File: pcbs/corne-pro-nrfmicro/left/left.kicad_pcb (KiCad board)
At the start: 2 copper layers, 131.6 x 87.7 mm, 53 parts, among them SW1 SW_PUSH-kbd, SW10 SW_PUSH-kbd, SW11 SW_PUSH-kbd, SW12 SW_PUSH-kbd, SW13 SW_PUSH-kbd, SW14 SW_PUSH-kbd, SW15 SW_PUSH-kbd, SW16 SW_PUSH-kbd, SW17 SW_PUSH-kbd, SW18 SW_PUSH-kbd, SW19 SW_PUSH-kbd, SW2 SW_PUSH-kbd, SW20 SW_PUSH-kbd, SW21 SW_PUSH-kbd, SW3 SW_PUSH-kbd, SW4 SW_PUSH-kbd, SW5 SW_PUSH-kbd, SW6 SW_PUSH-kbd, SW7 SW_PUSH-kbd, SW8 SW_PUSH-kbd, SW9 SW_PUSH-kbd, U1 ProMicro-kbd

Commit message: add gerber zip file
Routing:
- net GND: vias 3 -> 5
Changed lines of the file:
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@@
     (pad_to_mask_clearance 0)
     (pcbplotparams
-      (layerselection 0x0001000_7ffffffe)
+      (layerselection 0x00010fc_ffffffff)
       (disableapertmacros false)
-      (usegerberextensions false)
-      (usegerberattributes true)
-      (usegerberadvancedattributes true)
-      (creategerberjobfile true)
+      (usegerberextensions true)
+      (usegerberattributes false)
+      (usegerberadvancedattributes false)
+      (creategerberjobfile false)
       (svguseinch false)
       (svgprecision 6)
@@
       (psnegative false)
       (psa4output false)
-      (plotreference false)
+      (plotreference true)
       (plotvalue false)
       (plotinvisibletext false)
       (sketchpadsonfab false)
-      (subtractmaskfromsilk false)
-      (outputformat 3)
+      (subtractmaskfromsilk true)
+      (outputformat 1)
       (mirror false)
       (drillshape 0)
       (scaleselection 1)
-      (outputdirectory "/home/yong/kbd/split/mykeyboard/corne-pro/case/kicad-primitives/")
+      (outputdirectory "/home/yong/kbd-src/split/mykeyboard/pcbs/corne-pro-nrfmicro/left-gerber/")
     )
   )
@@
   (segment (start 195.208 61.316) (end 195.208 67.892) (width 0.4) (layer "F.Cu") (net 2))
   (segment (start 200.25 72.15) (end 200.25 80.3) (width 0.4) (layer "F.Cu") (net 2))
+  (via (at 200.075 64.275) (size 0.8) (drill 0.4) (layers "F.Cu" "B.Cu") (free) (net 2))
   (via (at 195.2 67.9) (size 0.8) (drill 0.4) (layers "F.Cu" "B.Cu") (net 2))
   (via (at 200.25 72.15) (size 0.8) (drill 0.4) (layers "F.Cu" "B.Cu") (net 2))
+  (via (at 200.075 85.275) (size 0.8) (drill 0.4) (layers "F.Cu" "B.Cu") (free) (net 2))
   (via (at 200.225 105.875) (size 0.8) (drill 0.4) (layers "F.Cu" "B.Cu") (net 2))
   (segment (start 199.75 67.9) (end 200.25 67.4) (width 0.4) (layer "B.Cu") (net 2))

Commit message: backup
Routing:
- net row4: track 81.7 -> 81.1 mm
- net GND: vias 5 -> 6

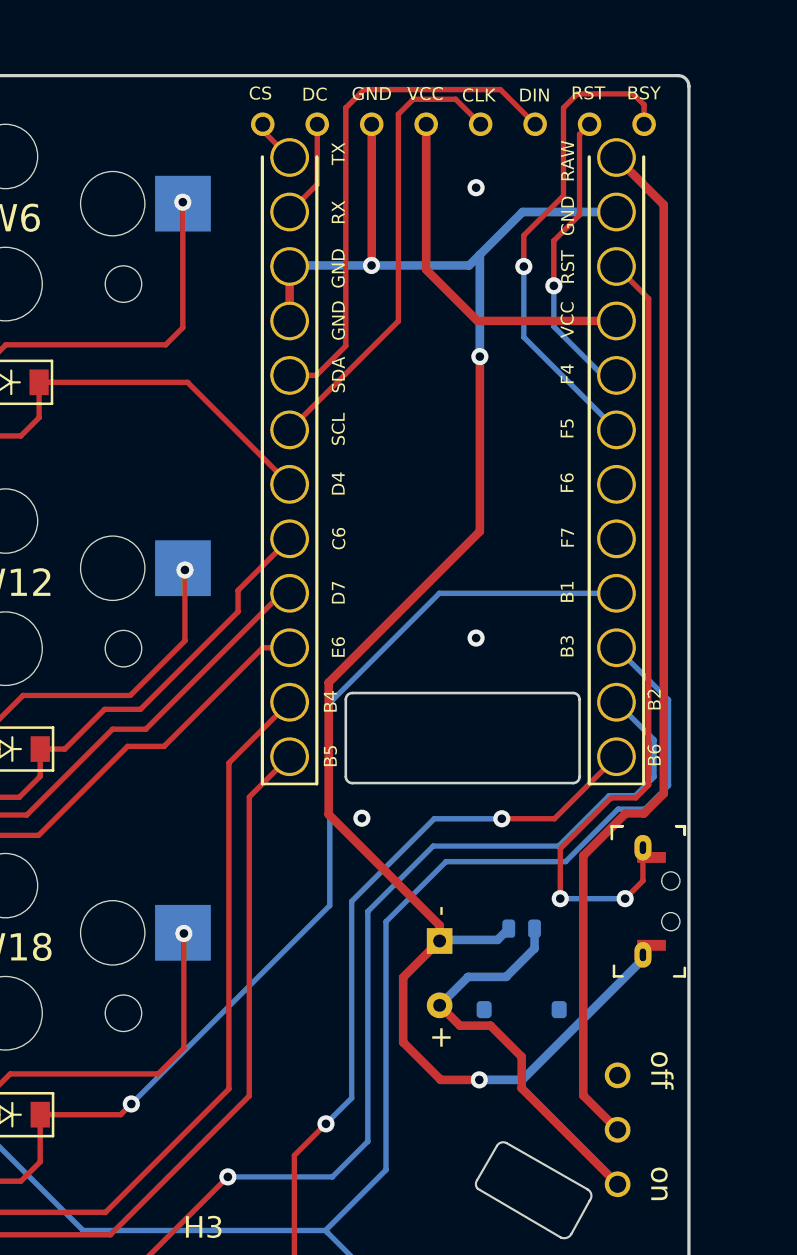
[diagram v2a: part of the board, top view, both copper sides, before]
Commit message: remove ground fill around anntena and tweak the anntena hole
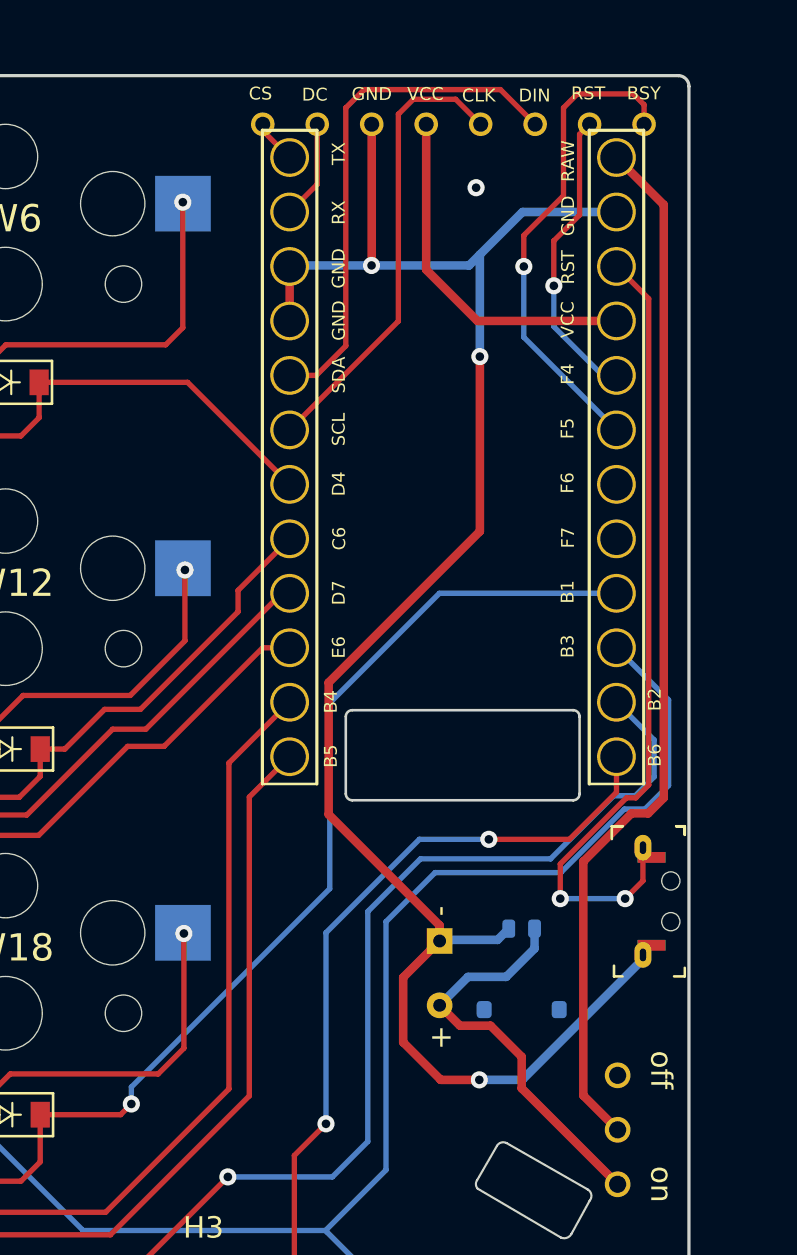
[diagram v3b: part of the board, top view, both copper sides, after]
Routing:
- net row4: track 81.1 -> 82.0 mm
- net GND: vias 6 -> 4
